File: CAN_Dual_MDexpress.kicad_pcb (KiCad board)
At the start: 2 copper layers, 85 x 100 mm, 160 parts, among them IC1 SI8650AB-B-IS1, IC2 A3921KLPTR-T, IC3 SI8650AB-B-IS1, IC4 A3921KLPTR-T, J1 PRT-10474, J2 Conn_01x02, J3 Conn_01x05, J4 PRT-10474, J5 Bus_PCIexpress_x16_164_Positi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, Q1 NVMFD5C650NLWFT1G, Q2 NVMFD5C650NLWFT1G, Q3 NVMFD5C650NLWFT1G, Q4 NVMFD5C650NLWFT1G, SW1 SW_Push, U1 LDO_3.3V, U2 STM32F042K6Tx, U3 MCP2562-E-SN

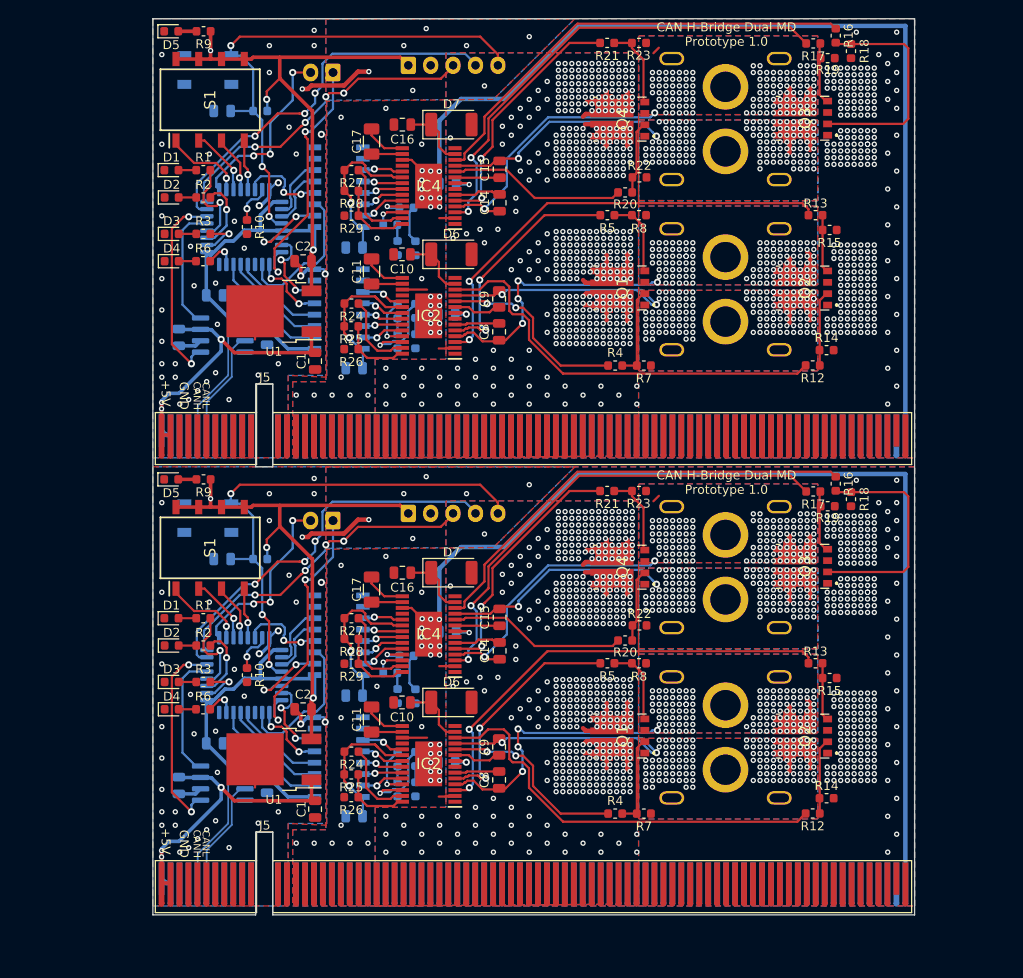
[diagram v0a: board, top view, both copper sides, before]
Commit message: Prototype1.2
Change: ST-LINK Conn, Rgs, Rg
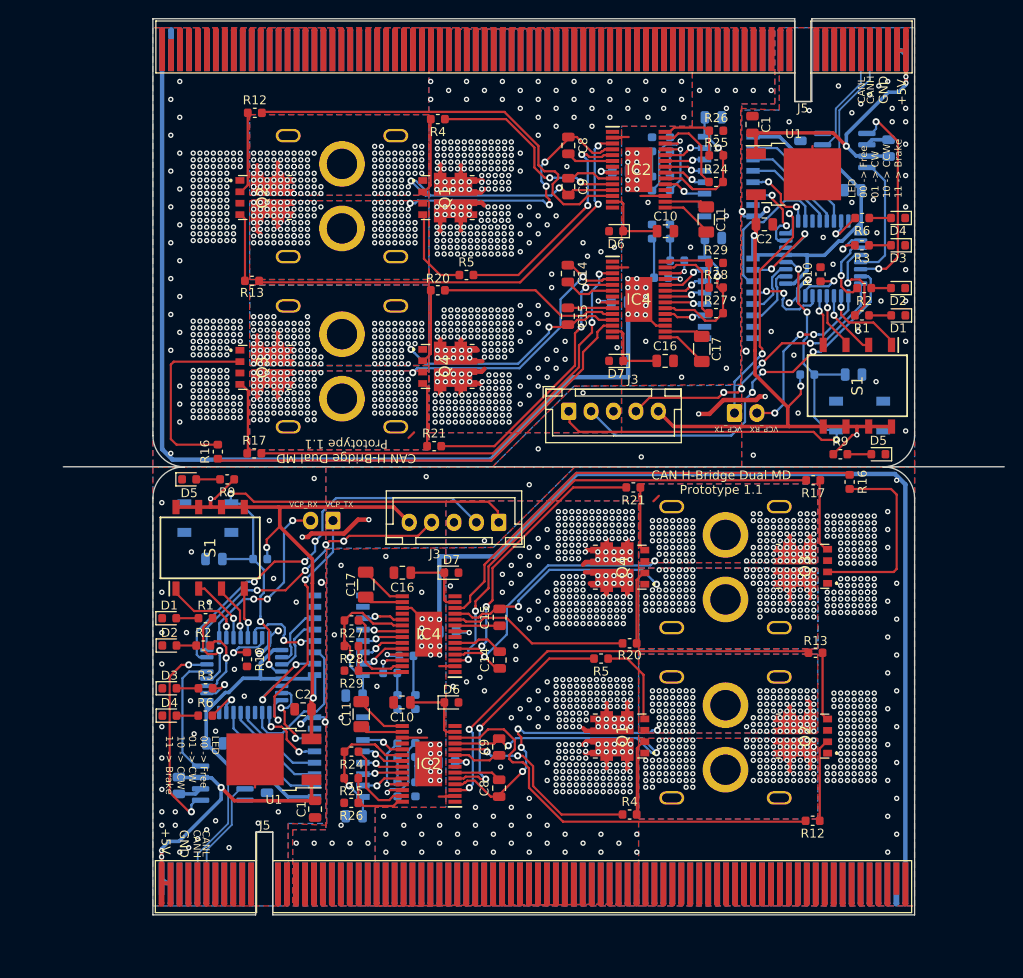
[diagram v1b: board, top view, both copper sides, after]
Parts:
- removed the D8 at (149.3, 60.6)
- removed the D8 at (149.3, 110.6)
- removed the D9 at (147.3, 60.6)
- removed the D9 at (147.3, 110.6)
- removed R14 (x2), R15 (x2), R18 (x2), R19 (x2), R22 (x2), R23 (x2), R7 (x2), R8 (x2): 10K, Resistor_SMD:R_0603_1608Metric
- removed the R30 at (148.3, 56.1)
- removed the R30 at (148.3, 106.1)
- added D8: LED, Diode_SMD:D_0603_1608Metric, B.Cu at (175.7, 58.8)
- added D8: LED, Diode_SMD:D_0603_1608Metric, B.Cu at (149.3, 111.2)
- added D9: LED, Diode_SMD:D_0603_1608Metric, B.Cu at (177.7, 58.8)
- added D9: LED, Diode_SMD:D_0603_1608Metric, B.Cu at (147.3, 111.2)
- added R30: 10K, Resistor_SMD:R_0603_1608Metric, B.Cu at (176.7, 63.9)
- added R30: 10K, Resistor_SMD:R_0603_1608Metric, B.Cu at (148.3, 106.1)
- D6 (x2), D7 (x2): footprint Diode_SMD:D_2010_5025Metric -> Diode_SMD:D_0603_1608Metric
- J3 (x2): moved to F.Cu
- R12 (x2), R13 (x2), R16 (x2), R17 (x2), R20 (x2), R21 (x2), R4 (x2), R5 (x2): value 100 -> 21
- R24 (x2), R27 (x2): value 30K -> 3K
- moved J5 93.0 mm to (204.0, 39.0), turned to 180 degrees
- moved D5 91.9 mm to (201.0, 83.6), turned to 180 degrees
- moved R9 85.3 mm to (196.7, 83.6), turned to 0 degrees
- moved R16 83.1 mm to (127.2, 83.3), turned to 90 degrees
- moved D1 82.7 mm to (203.2, 68.1), turned to 180 degrees
- moved SW1 82.3 mm to (198.9, 79.3), turned to 0 degrees
- moved C6 82.0 mm to (202.1, 49.4), turned to 270 degrees
- moved D2 81.7 mm to (203.2, 65.1), turned to 180 degrees
- moved D4 81.2 mm to (203.2, 57.2), turned to 180 degrees
- moved D3 81.1 mm to (203.2, 60.3), turned to 180 degrees
- moved S1 79.0 mm to (198.6, 76.0), turned to 270 degrees
- moved R17 77.4 mm to (131.3, 83.5), turned to 0 degrees
- moved C3 76.3 mm to (198.2, 74.7), turned to 0 degrees
- moved R1 75.3 mm to (199.1, 68.1), turned to 180 degrees
- moved R2 74.4 mm to (199.4, 65.1), turned to 180 degrees
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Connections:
- J3 pad 1: +3V3 -> NRST (x2)
- J3 pad 2: GND -> /SWDIO (x2)
- J3 pad 3: /SWCLK -> GND (x2)
- J3 pad 4: /SWDIO -> /SWCLK (x2)
- J3 pad 5: NRST -> +3V3 (x2)
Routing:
- net Net-(Q3-Pad2): track 50.9 -> 42.9 mm
- net /SWCLK: track 72.1 -> 65.8 mm
- net GHB_0: track 55.9 -> 61.9 mm
- net VCC: track 32.5 -> 36.4 mm, vias 908 -> 822
- net GND: track 46.2 -> 42.4 mm, vias 88 -> 82
- net +3V3: track 206.1 -> 209.7 mm
- net Net-(Q1-Pad2): track 20.2 -> 17.0 mm
- net Net-(Q4-Pad4): track 18.5 -> 15.4 mm
- net GHA_1: track 42.9 -> 46.0 mm
- net IC_RESET_0: track 18.0 -> 21.0 mm
- net GLB_0: track 107.2 -> 104.3 mm
- net GLA_0: track 101.0 -> 103.8 mm
- net Net-(C11-Pad2): track 6.89 -> 9.68 mm
- net Net-(Q3-Pad4): track 14.3 -> 16.8 mm
- net /BOOT: track 9.03 -> 11.5 mm
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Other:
- board size 85 x 100 mm -> 105 x 100 mm
- board text added: "+3V3"
- board text added: "CAN H-Bridge Dual MD Prototype 1.1"
- board text added: "LED 00 -> Free 01 -> CW 10 -> CCW 11 -> Brake"
- board text added: "MD0"
- board text added: "MD1"
- board text added: "NRST"
- board text added: "SWCLK"
- board text added: "SWDIO"
- board text added: "VCP_RX"
- board text added: "VCP_TX"
- board text removed: "CAN H-Bridge Dual MD Prototype 1.0"

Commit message: add 3V3LDO & pad
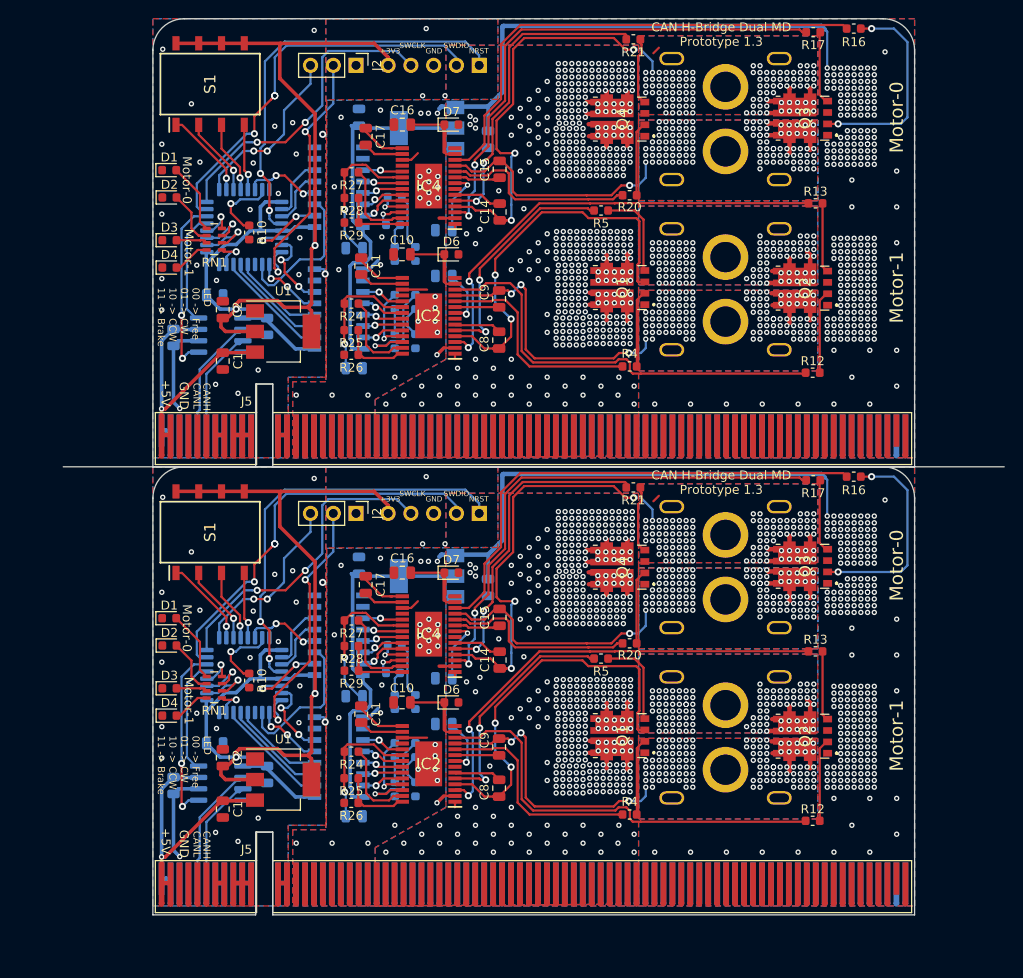
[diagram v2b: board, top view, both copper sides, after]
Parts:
- removed the C3 at (198.2, 74.7)
- removed the C3 at (126.8, 95.3)
- removed D5 (x2): LED, Diode_SMD:D_0603_1608Metric
- removed the J1 at (141.1, 54.8)
- removed the J1 at (183.9, 115.2)
- removed the J2 at (184.9, 79.0)
- removed the J2 at (140.1, 91.0)
- removed the J4 at (141.1, 73.8)
- removed the J4 at (183.9, 96.2)
- removed the J5 at (204.0, 39.0)
- removed the J5 at (121.0, 130.9)
- removed the Q1 at (152.6, 55.0)
- removed the Q1 at (172.4, 115.0)
- removed the Q2 at (132.2, 55.0)
- removed the Q2 at (192.8, 115.0)
- removed R1 (x2), R2 (x2), R3 (x2), R6 (x2): 2.2K, Resistor_SMD:R_0603_1608Metric
- removed R11 (x2), R9 (x2): 10K, Resistor_SMD:R_0603_1608Metric
- removed SW1 (x2): SW_Push, SamacSys_Parts:PTS647SM38SMTR2LFS
- removed the U1 at (191.5, 52.4)
- removed the U1 at (133.5, 117.6)
- added C19: 4.7uF, Capacitor_SMD:C_0805_2012Metric, B.Cu at (143.0, 46.0)
- added C19: 4.7uF, Capacitor_SMD:C_0805_2012Metric, B.Cu at (143.0, 96.0)
- added C3: 1uF, Capacitor_SMD:C_0805_2012Metric, B.Cu at (157.4, 48.5)
- added C3: 1uF, Capacitor_SMD:C_0805_2012Metric, B.Cu at (157.4, 98.5)
- added J1: Conn_01x02, XT60:XT60PW_Reversible, B.Cu at (183.9, 65.2)
- added J1: Conn_01x02, XT60:XT60PW_Reversible, B.Cu at (183.9, 115.2)
- added J2: Conn_01x03, Connector_PinHeader_2.54mm:PinHeader_1x03_P2.54mm_Vertical, F.Cu at (142.7, 40.2)
- added J2: Conn_01x03, Connector_PinHeader_2.54mm:PinHeader_1x03_P2.54mm_Vertical, F.Cu at (142.7, 90.2)
- added J4: Conn_01x02, XT60:XT60PW_Reversible, B.Cu at (183.9, 46.2)
- added J4: Conn_01x02, XT60:XT60PW_Reversible, B.Cu at (183.9, 96.2)
- added J5: Bus_mechaken_PCIexpress_x16_164_Position, PCIe:BUS_mechaken_PCIexpress_x16_164_Position, F.Cu at (121.0, 81.0)
- added J5: Bus_mechaken_PCIexpress_x16_164_Position, PCIe:BUS_mechaken_PCIexpress_x16_164_Position, F.Cu at (121.0, 130.9)
- added Q1: NVMFD5C446NT1G, SamacSys_Parts:NVMFD5C446NLWFT1G, F.Cu at (172.4, 65.0)
- added Q1: NVMFD5C446NT1G, SamacSys_Parts:NVMFD5C446NLWFT1G, F.Cu at (172.4, 115.0)
- added Q2: NVMFD5C446NT1G, SamacSys_Parts:NVMFD5C446NLWFT1G, F.Cu at (192.8, 65.1)
- added Q2: NVMFD5C446NT1G, SamacSys_Parts:NVMFD5C446NLWFT1G, F.Cu at (192.8, 115.1)
- added RN1: R_Pack04, Resistor_SMD:R_Array_Concave_4x0603, F.Cu at (126.8, 59.6)
- added RN1: R_Pack04, Resistor_SMD:R_Array_Concave_4x0603, F.Cu at (126.8, 109.6)
- added U1: LDL1117S33TR_SOT223-4, Package_TO_SOT_SMD:SOT-223-3_TabPin2, F.Cu at (134.6, 69.9)
- added U1: LDL1117S33TR_SOT223-4, Package_TO_SOT_SMD:SOT-223-3_TabPin2, F.Cu at (134.6, 119.9)
- added U4: LDL1117S33TR_SOT223-4, Package_TO_SOT_SMD:SOT-223-3_TabPin2, B.Cu at (150.6, 47.2)
- added U4: LDL1117S33TR_SOT223-4, Package_TO_SOT_SMD:SOT-223-3_TabPin2, B.Cu at (150.6, 97.2)
- C1 (x2): value 0.1uF -> 1uF
- C11 (x2), C17 (x2): footprint Capacitor_SMD:C_1206_3216Metric -> Capacitor_SMD:C_0805_2012Metric
- C2 (x2): value 0.1uF -> 4.7uF
- D1 (x2), D10 (x2), D11 (x2), D2 (x2), D3 (x2), D4 (x2), D8 (x2), D9 (x2): footprint Diode_SMD:D_0603_1608Metric -> LED_SMD:LED_0603_1608Metric
- J3 (x2): footprint Connector_JST:JST_XH_B5B-XH-A_1x05_P2.50mm_Vertical -> Connector_PinHeader_2.54mm:PinHeader_1x05_P2.54mm_Vertical; moved to B.Cu
- Q3 (x2), Q4 (x2): value NVMFD5C650NLWFT1G -> NVMFD5C446NT1G
- moved R16 85.2 mm to (198.2, 36.1), turned to 0 degrees
- moved D1 83.0 mm to (121.8, 51.9), turned to 0 degrees
- moved C6 82.5 mm to (122.3, 70.6), turned to 90 degrees
- moved D2 81.9 mm to (121.8, 54.9), turned to 0 degrees
- moved D4 81.5 mm to (121.8, 62.8), turned to 0 degrees
- moved D3 81.3 mm to (121.8, 59.7), turned to 0 degrees
- moved S1 79.7 mm to (126.4, 42.3), turned to 90 degrees
- moved R17 78.1 mm to (193.7, 36.5), turned to 180 degrees
- moved U3 72.6 mm to (127.6, 70.3), turned to 0 degrees
- moved C4 72.2 mm to (126.9, 65.9), turned to 180 degrees
- moved R12 68.7 mm to (193.6, 74.5), turned to 0 degrees
- moved Q3 66.7 mm to (192.8, 46.1), turned to 90 degrees
- moved C1 64.7 mm to (127.8, 73.2), turned to 270 degrees
- moved U2 64.7 mm to (130.2, 58.2), turned to 180 degrees
- moved R10 63.9 mm to (130.8, 58.9), turned to 270 degrees
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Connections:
- C12 pad 1: MD_V5_1 -> Net-(C12-Pad1) (x2)
- C18 pad 1: MD_V5_0 -> Net-(C18-Pad1) (x2)
- C9 pad 1: Net-(C9-Pad1) -> SA_1 (x2)
- C9 pad 2: SA_1 -> Net-(C9-Pad2) (x2)
- IC1 pad 16: MD_V5_1 -> MD_3V3 (x2)
- IC2 pad 20: MD_V5_1 -> Net-(C12-Pad1) (x2)
- IC2 pad 9: Net-(C9-Pad1) -> Net-(C9-Pad2) (x2)
- IC3 pad 16: MD_V5_0 -> MD_3V3 (x2)
- IC4 pad 20: MD_V5_0 -> Net-(C18-Pad1) (x2)
- Q3 pad 6: SB_0 -> SA_0 (x2)
- R24 pad 2: MD_V5_1 -> Net-(C12-Pad1) (x2)
- R25 pad 2: MD_V5_1 -> Net-(C12-Pad1) (x2)
- R27 pad 2: MD_V5_0 -> Net-(C18-Pad1) (x2)
- R28 pad 2: MD_V5_0 -> Net-(C18-Pad1) (x2)
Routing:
- net GNDPWR: track 247.3 -> 138.9 mm, vias 492 -> 510
- net MD_3V3: track 0.00 -> 81.4 mm
- net SB_0: track 68.6 -> 116.1 mm, vias 242 -> 218
- net SB_1: track 67.3 -> 105.3 mm, vias 236 -> 206
- net MD_V5_0: track 34.1 -> 0.00 mm, vias 2 -> 0
- net Net-(C18-Pad1): track 0.00 -> 33.8 mm, vias 0 -> 2
- net MD_V5_1: track 31.9 -> 0.00 mm, vias 2 -> 0
- net Net-(C12-Pad1): track 0.00 -> 29.2 mm, vias 0 -> 2
- net +3V3: track 209.7 -> 238.9 mm, vias 6 -> 4
- net NRST: track 117.5 -> 92.7 mm, vias 6 -> 4
- net SA_1: track 58.7 -> 79.1 mm, vias 256 -> 232
- net SA_0: track 55.6 -> 74.3 mm, vias 250 -> 214
- net GND: track 42.4 -> 23.9 mm, vias 82 -> 54
- net VCC: track 36.4 -> 52.1 mm, vias 822 -> 870
- net MD0_LED_H: track 19.3 -> 6.57 mm
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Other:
- outline, holes or cut-outs redrawn
- board text added: "CAN H-Bridge Dual MD Prototype 1.3"
- board text added: "Motor-0"
- board text added: "Motor-1"
- board text removed: "CAN H-Bridge Dual MD Prototype 1.1"
- board text removed: "MD0"
- board text removed: "MD1"

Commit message: Prototype 1.3
FusionPCB(12/12)
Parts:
- removed D11: LED, LED_SMD:LED_0603_1608Metric
- removed R20, R21: 21, Resistor_SMD:R_0603_1608Metric
- removed R24, R27: 3K, Resistor_SMD:R_0603_1608Metric
- removed R25, R28: 3.74k, Resistor_SMD:R_0603_1608Metric
- removed R26, R29: 1.2k, Resistor_SMD:R_0603_1608Metric
- removed R30, R31, R32, R33: 10K, Resistor_SMD:R_0603_1608Metric
- added D5: D, Diode_SMD:D_0603_1608Metric, F.Cu at (148.3, 66.3)
- added R1: 21, Resistor_SMD:R_0603_1608Metric, F.Cu at (168.2, 78.8)
- added R11: 10K, Resistor_SMD:R_0603_1608Metric, B.Cu at (141.8, 63.0)
- added R14: 3K, Resistor_SMD:R_0603_1608Metric, F.Cu at (137.2, 71.8)
- added R15: 3.74k, Resistor_SMD:R_0603_1608Metric, F.Cu at (137.1, 74.8)
- added R18: 3.74k, Resistor_SMD:R_0603_1608Metric, F.Cu at (137.2, 60.0)
- added R19: 1.2k, Resistor_SMD:R_0603_1608Metric, F.Cu at (137.2, 62.8)
- added R2: 21, Resistor_SMD:R_0603_1608Metric, F.Cu at (165.0, 61.4)
- added R3: 10K, Resistor_SMD:R_0603_1608Metric, F.Cu at (125.8, 63.9)
- added R6: 21, Resistor_SMD:R_0603_1608Metric, F.Cu at (193.2, 41.1)
- added R7: 21, Resistor_SMD:R_0603_1608Metric, F.Cu at (188.7, 41.5)
- added R8: 10K, Resistor_SMD:R_0603_1608Metric, B.Cu at (142.0, 71.6)
- added R9: 10K, Resistor_SMD:R_0603_1608Metric, B.Cu at (144.3, 71.6)
- C10: value 0.1uF -> 0.47uF
- C11: value 0.47uF -> 0.1uF; moved to B.Cu
- C12, C6: value 0.1uF -> 4.7uF
- C13, C7: value 4.7uF -> 0.1uF; moved to F.Cu
- C16: value 0.1uF -> 1uF; moved to B.Cu
- C17: value 0.47uF -> 4.7uF; moved to B.Cu
- C18: value 0.1uF -> 0.47uF; moved to F.Cu
- C19: value 4.7uF -> 0.1uF
- C3: value 1uF -> 0.1uF
- D10: value LED -> D; footprint LED_SMD:LED_0603_1608Metric -> Diode_SMD:D_0603_1608Metric; moved to F.Cu
- D6, D7: value D -> LED; footprint Diode_SMD:D_0603_1608Metric -> LED_SMD:LED_0603_1608Metric; moved to B.Cu
- R10: moved to B.Cu
- R16: value 21 -> 1.2k
- R17: value 21 -> 3K
- moved R16 73.8 mm to (137.1, 77.5), turned to 180 degrees
- moved R17 60.2 mm to (137.2, 57.1)
- moved C3 42.0 mm to (121.9, 70.9), turned to 180 degrees
- moved D7 30.5 mm to (144.3, 76.0), turned to 90 degrees
- moved R12 29.4 mm to (168.2, 59.7)
- moved R13 28.6 mm to (168.6, 42.3)
- moved C6 25.2 mm to (147.5, 68.7), turned to 180 degrees
- moved C19 20.4 mm to (137.5, 65.6), turned to 180 degrees
- moved R5 19.4 mm to (188.9, 60.6)
- moved D10 19.2 mm to (148.3, 51.8), turned to 0 degrees
- moved D6 18.5 mm to (142.0, 76.0), turned to 90 degrees
- moved C11 17.8 mm to (137.5, 79.4), turned to 0 degrees
- moved C5 16.6 mm to (117.3, 75.6)
- moved R4 16.4 mm to (188.6, 79.5)
- moved C15 15.9 mm to (142.8, 51.8), turned to 180 degrees
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- renumbered C11 to C10, C12 to C11, C13 to C12, C14 to C13, C15 to C14, C16 to C15, C3 to C16, C19 to C17, C17 to C18, C18 to C19, C4 to C3, C5 to C4, C6 to C5, C7 to C6, C8 to C7, C9 to C8, C10 to C9, D7 to D10, D6 to D5, D10 to D6, D11 to D7, R4 to R1, R30 to R10, R31 to R11, R20 to R12, R21 to R13, R24 to R14, R25 to R15, R26 to R16, R27 to R17, R28 to R18, R29 to R19, R5 to R2, R10 to R3, R12 to R4, R13 to R5, R16 to R6, R17 to R7, R32 to R8, R33 to R9
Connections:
- C10 pad 2: GNDPWR -> Net-(C10-Pad2)
- C10 pad 1: Net-(C11-Pad1) -> Net-(C10-Pad1)
- C10 pad 2: Net-(C11-Pad2) -> Net-(C10-Pad2)
- C11 pad 2: Net-(C11-Pad2) -> GNDPWR
- C11 pad 1: Net-(C12-Pad1) -> Net-(C11-Pad1)
- C12 pad 1: Net-(C12-Pad1) -> VREG_0
- C13 pad 1: VREG_0 -> SB_0
- C13 pad 2: GNDPWR -> Net-(C13-Pad2)
- C13 pad 2: Net-(C14-Pad2) -> Net-(C13-Pad2)
- C14 pad 1: SB_0 -> Net-(C14-Pad1)
- C14 pad 2: Net-(C14-Pad2) -> SA_0
- C14 pad 1: Net-(C15-Pad1) -> Net-(C14-Pad1)
- C15 pad 2: SA_0 -> GNDPWR
- C15 pad 1: Net-(C16-Pad1) -> Net-(C15-Pad1)
- C16 pad 1: Net-(C16-Pad1) -> VCC
- C17 pad 1: Net-(C17-Pad1) -> GNDPWR
- C17 pad 2: Net-(C17-Pad2) -> MD_3V3
- C18 pad 2: GNDPWR -> Net-(C18-Pad2)
- C18 pad 1: Net-(C17-Pad1) -> Net-(C18-Pad1)
- C18 pad 2: Net-(C17-Pad2) -> Net-(C18-Pad2)
- C19 pad 1: GNDPWR -> Net-(C19-Pad1)
- C19 pad 2: MD_3V3 -> GNDPWR
- C19 pad 1: Net-(C18-Pad1) -> Net-(C19-Pad1)
- C3 pad 1: VCC -> GND
- C3 pad 2: GNDPWR -> +3V3
- C5 pad 2: +3V3 -> +5V
- C6 pad 1: GND -> VREG_1
- C6 pad 2: +5V -> GNDPWR
- C7 pad 1: VREG_1 -> SB_1
- C7 pad 2: GNDPWR -> Net-(C7-Pad2)
- C7 pad 2: Net-(C8-Pad2) -> Net-(C7-Pad2)
- C8 pad 1: SB_1 -> SA_1
- C8 pad 2: Net-(C9-Pad2) -> Net-(C8-Pad2)
- C9 pad 1: SA_1 -> Net-(C9-Pad1)
- C9 pad 2: Net-(C9-Pad2) -> GNDPWR
- C9 pad 1: Net-(C10-Pad1) -> Net-(C9-Pad1)
- D10 pad 1: GNDPWR -> Net-(C15-Pad1)
- D10 pad 2: Net-(D10-Pad2) -> VCC
- D10 pad 1: Net-(C16-Pad1) -> Net-(C15-Pad1)
- D5 pad 1: Net-(C10-Pad1) -> Net-(C9-Pad1)
- D6 pad 1: Net-(C10-Pad1) -> GNDPWR
- D6 pad 2: VCC -> Net-(D6-Pad2)
- D6 pad 2: Net-(D10-Pad2) -> Net-(D6-Pad2)
- D7 pad 1: Net-(C16-Pad1) -> GNDPWR
- D7 pad 2: VCC -> Net-(D7-Pad2)
- D7 pad 2: Net-(D11-Pad2) -> Net-(D7-Pad2)
- IC2 pad 13: Net-(C10-Pad1) -> Net-(C9-Pad1) (x2)
- IC2 pad 15: Net-(C11-Pad1) -> Net-(C10-Pad1) (x2)
- IC2 pad 16: Net-(C11-Pad2) -> Net-(C10-Pad2) (x2)
- IC2 pad 20: Net-(C12-Pad1) -> Net-(C11-Pad1) (x2)
- IC2 pad 6: Net-(C8-Pad2) -> Net-(C7-Pad2) (x2)
- IC2 pad 9: Net-(C9-Pad2) -> Net-(C8-Pad2) (x2)
- IC4 pad 13: Net-(C16-Pad1) -> Net-(C15-Pad1) (x2)
- IC4 pad 15: Net-(C17-Pad1) -> Net-(C18-Pad1) (x2)
- IC4 pad 16: Net-(C17-Pad2) -> Net-(C18-Pad2) (x2)
- IC4 pad 20: Net-(C18-Pad1) -> Net-(C19-Pad1) (x2)
- IC4 pad 6: Net-(C14-Pad2) -> Net-(C13-Pad2) (x2)
- IC4 pad 9: Net-(C15-Pad1) -> Net-(C14-Pad1) (x2)
- R10 pad 1: /BOOT -> MD_FF1_0
- R10 pad 2: GND -> Net-(D8-Pad2)
- R12 pad 1: GLA_1 -> GHA_0
- R12 pad 2: Net-(Q2-Pad2) -> Net-(Q4-Pad2)
- R13 pad 1: Net-(Q2-Pad4) -> Net-(Q4-Pad4)
- R13 pad 2: GLB_1 -> GHB_0
- R14 pad 2: Net-(C12-Pad1) -> Net-(C11-Pad1)
- R15 pad 2: Net-(C12-Pad1) -> Net-(C11-Pad1)
- R16 pad 1: GLA_0 -> Net-(IC2-Pad28)
- R16 pad 2: Net-(Q3-Pad2) -> GNDPWR
- R17 pad 1: Net-(Q3-Pad4) -> Net-(IC4-Pad27)
- R17 pad 2: GLB_0 -> Net-(C19-Pad1)
- R17 pad 2: Net-(C18-Pad1) -> Net-(C19-Pad1)
- R18 pad 2: Net-(C18-Pad1) -> Net-(C19-Pad1)
- R4 pad 1: GHA_1 -> GLA_1
- R4 pad 2: Net-(Q1-Pad2) -> Net-(Q2-Pad2)
- R5 pad 1: Net-(Q1-Pad4) -> Net-(Q2-Pad4)
- R5 pad 2: GHB_1 -> GLB_1
- R8 pad 2: Net-(D10-Pad2) -> Net-(D6-Pad2)
- R9 pad 2: Net-(D11-Pad2) -> Net-(D7-Pad2)
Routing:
- net Net-(C19-Pad1): track 0.00 -> 36.0 mm, vias 0 -> 2
- net Net-(C12-Pad1): track 29.2 -> 0.00 mm, vias 2 -> 0
- net Net-(C18-Pad1): track 33.8 -> 11.0 mm, vias 2 -> 0
- net Net-(C9-Pad1): track 0.00 -> 22.3 mm
- net Net-(C16-Pad1): track 22.3 -> 0.00 mm
- net Net-(C11-Pad1): track 11.4 -> 32.8 mm, vias 0 -> 2
- net Net-(C17-Pad2): track 15.2 -> 0.00 mm
- net Net-(C18-Pad2): track 0.00 -> 15.2 mm
- net Net-(C15-Pad1): track 9.33 -> 22.3 mm
- net Net-(C17-Pad1): track 11.0 -> 0.00 mm
- net Net-(C10-Pad1): track 22.3 -> 11.4 mm
- net Net-(C14-Pad2): track 10.8 -> 0.00 mm
- net Net-(C13-Pad2): track 0.00 -> 10.8 mm
- net Net-(C7-Pad2): track 0.00 -> 10.5 mm
- net Net-(C10-Pad2): track 0.00 -> 10.2 mm
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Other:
- board text added: "CAN H-Bridge Dual MD Prototype 1.2"
- board text removed: "CAN H-Bridge Dual MD Prototype 1.3"
